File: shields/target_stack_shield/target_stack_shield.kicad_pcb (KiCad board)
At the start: 4 copper layers, 85 x 56 mm, 17 parts, among them IC1 NCP1117DT33T5G, J1 Probe Channel 0, J2 Probe Channel 1, J3 Probe Channel 2, J4 Probe Channel 3, J5 GPIO shield connector 40pin, J6 probe shield connector 20 or 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

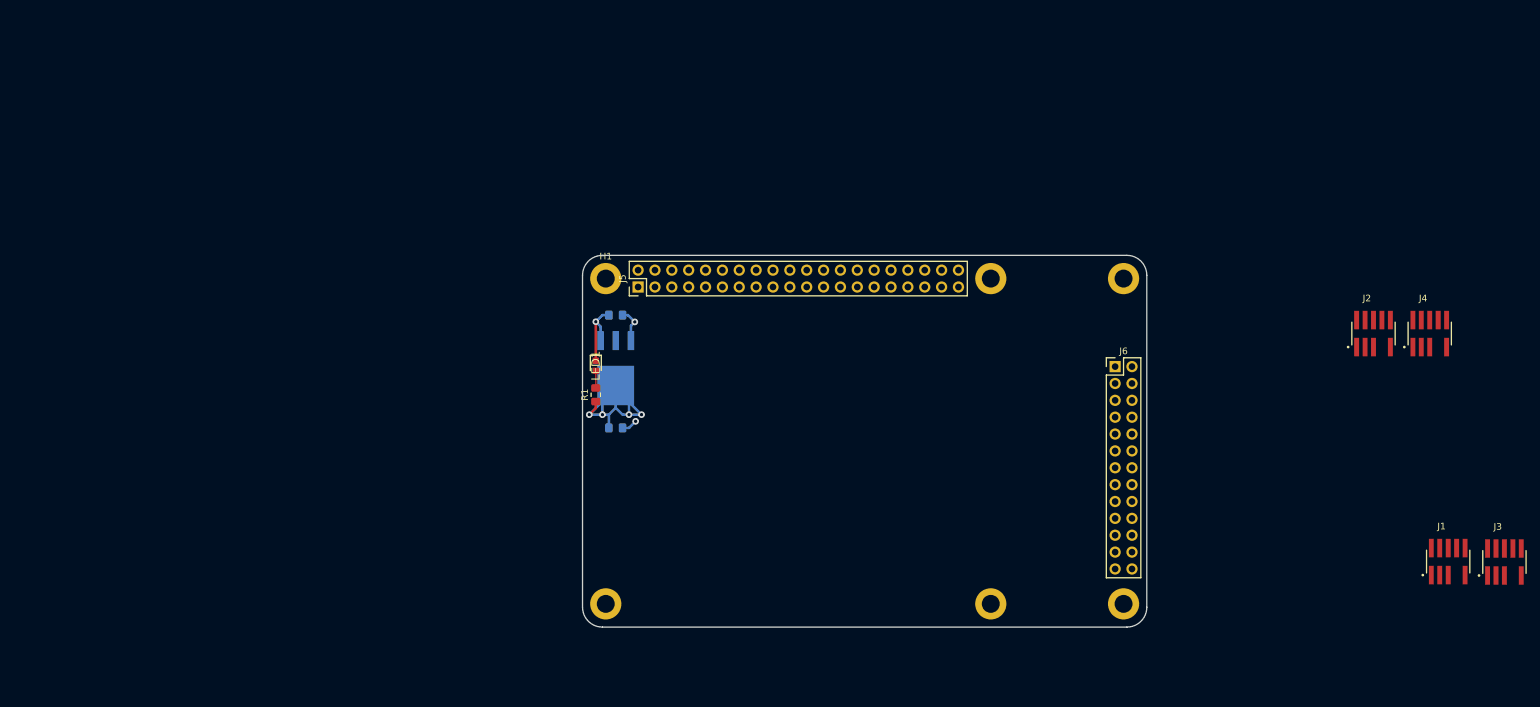
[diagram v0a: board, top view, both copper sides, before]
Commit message: work on target stack shield layout
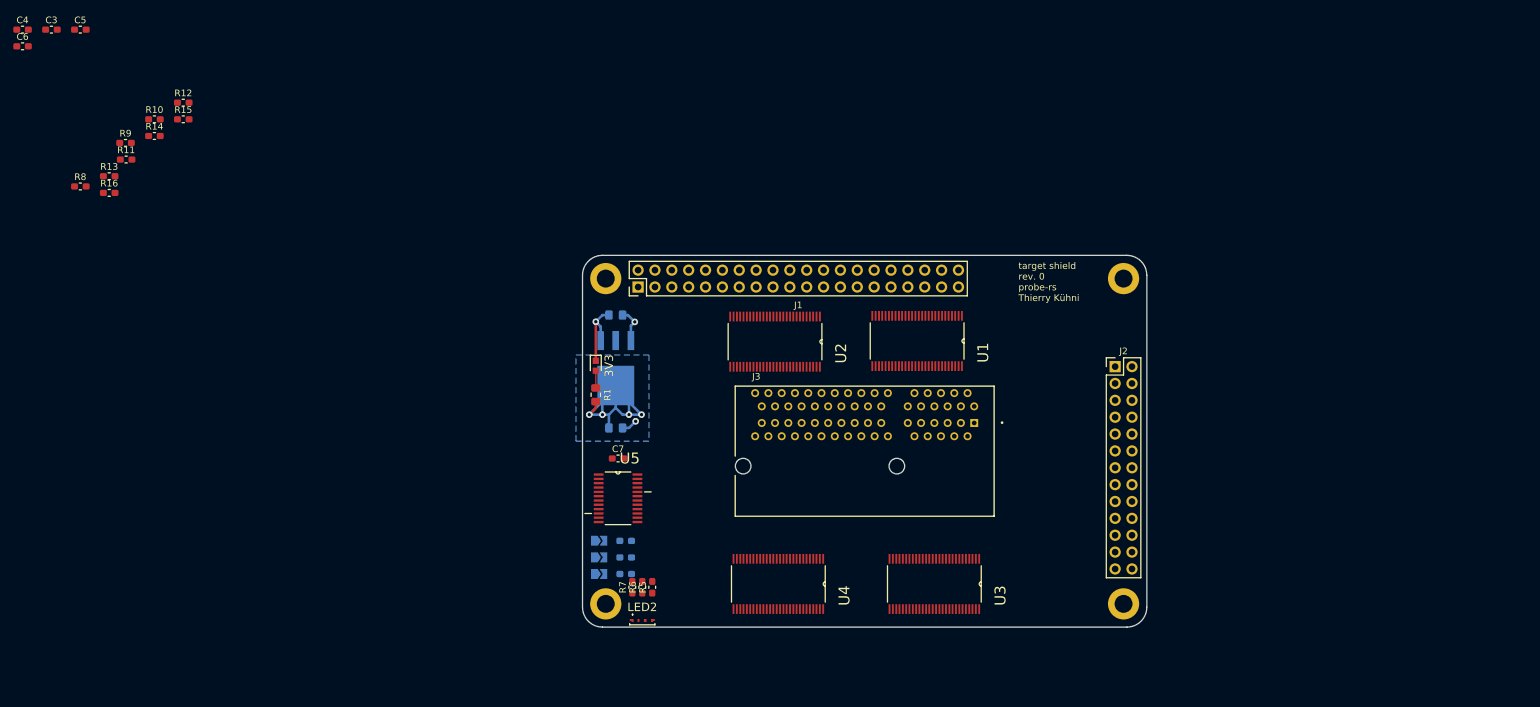
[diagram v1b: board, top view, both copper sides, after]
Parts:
- removed H5, H6: MountingHole, MountingHole:MountingHole_2.7mm_M2.5_DIN965_Pad
- removed J4: Probe Channel 3, hive:SAMTEC_FTSH-105-01-F-DV-007
- removed J5: GPIO shield connector 40pin, Connector_PinHeader_2.54mm:PinHeader_2x20_P2.54mm_Vertical
- removed J6: probe shield connector 20 or 26pin, Connector_PinHeader_2.54mm:PinHeader_2x13_P2.54mm_Vertical
- removed LED1: 3.3V OK (green), hive:LEDC1608X80N
- added 3V3: 3.3V OK (green), hive:LEDC1608X80N, F.Cu at (112.0, 70.6)
- added C3: 100n, Capacitor_SMD:C_0603_1608Metric_Pad1.05x0.95mm_HandSolder, F.Cu at (30.0, 20.0)
- added C4: 100n, Capacitor_SMD:C_0603_1608Metric_Pad1.05x0.95mm_HandSolder, F.Cu at (25.6, 20.0)
- added C5: 100n, Capacitor_SMD:C_0603_1608Metric_Pad1.05x0.95mm_HandSolder, F.Cu at (34.4, 20.0)
- added C6: 100n, Capacitor_SMD:C_0603_1608Metric_Pad1.05x0.95mm_HandSolder, F.Cu at (25.6, 22.5)
- added C7: 100n, Capacitor_SMD:C_0603_1608Metric_Pad1.05x0.95mm_HandSolder, F.Cu at (115.3, 84.6)
- added JP1: Address Bit 0, Jumper:SolderJumper-2_P1.3mm_Open_TrianglePad1.0x1.5mm, B.Cu at (112.5, 102.0)
- added JP2: Address Bit 1, Jumper:SolderJumper-2_P1.3mm_Open_TrianglePad1.0x1.5mm, B.Cu at (112.5, 99.5)
- added JP3: Address Bit 2, Jumper:SolderJumper-2_P1.3mm_Open_TrianglePad1.0x1.5mm, B.Cu at (112.5, 97.0)
- added LED2: KRTB_AILMS1-5B5C-B1B12-0-R18, hive:KRTBAILMS15B5CB1B120R18, F.Cu at (119.0, 109.2)
- added R10: 100k, Resistor_SMD:R_0603_1608Metric_Pad1.05x0.95mm_HandSolder, F.Cu at (45.5, 33.5)
- added R11: 100k, Resistor_SMD:R_0603_1608Metric_Pad1.05x0.95mm_HandSolder, F.Cu at (41.2, 39.6)
- added R12: 100k, Resistor_SMD:R_0603_1608Metric_Pad1.05x0.95mm_HandSolder, F.Cu at (49.9, 31.0)
- added R13: 100k, Resistor_SMD:R_0603_1608Metric_Pad1.05x0.95mm_HandSolder, F.Cu at (38.7, 42.1)
- added R14: 100k, Resistor_SMD:R_0603_1608Metric_Pad1.05x0.95mm_HandSolder, F.Cu at (45.5, 36.0)
- added R15: 100k, Resistor_SMD:R_0603_1608Metric_Pad1.05x0.95mm_HandSolder, F.Cu at (49.9, 33.5)
- added R16: 100k, Resistor_SMD:R_0603_1608Metric_Pad1.05x0.95mm_HandSolder, F.Cu at (38.7, 44.6)
- added R2: 100k, Resistor_SMD:R_0603_1608Metric_Pad1.05x0.95mm_HandSolder, B.Cu at (116.5, 102.0)
- added R3: 100k, Resistor_SMD:R_0603_1608Metric_Pad1.05x0.95mm_HandSolder, B.Cu at (116.5, 99.5)
- added R4: 100k, Resistor_SMD:R_0603_1608Metric_Pad1.05x0.95mm_HandSolder, B.Cu at (116.5, 97.0)
- added R5: 150, Resistor_SMD:R_0603_1608Metric_Pad1.05x0.95mm_HandSolder, F.Cu at (120.5, 104.0)
- added R6: 45, Resistor_SMD:R_0603_1608Metric_Pad1.05x0.95mm_HandSolder, F.Cu at (119.0, 104.0)
- added R7: 30, Resistor_SMD:R_0603_1608Metric_Pad1.05x0.95mm_HandSolder, F.Cu at (117.5, 104.0)
- added R8: 100k, Resistor_SMD:R_0603_1608Metric_Pad1.05x0.95mm_HandSolder, F.Cu at (34.4, 43.6)
- added R9: 100k, Resistor_SMD:R_0603_1608Metric_Pad1.05x0.95mm_HandSolder, F.Cu at (41.2, 37.1)
- added U1: SN74CB3T16211DGGR, hive:SOP50P810X120-56N, F.Cu at (160.4, 66.9)
- added U2: SN74CB3T16211DGGR, hive:SOP50P810X120-56N, F.Cu at (139.0, 67.0)
- added U3: SN74CB3T16211DGGR, hive:SOP50P810X120-56N, F.Cu at (163.0, 103.5)
- added U4: SN74CB3T16211DGGR, hive:SOP50P810X120-56N, F.Cu at (139.5, 103.5)
- added U5: PCA9535CPW,118, hive:SOP65P640X110-24N, F.Cu at (115.3, 90.6)
- H1, H2, H3, H4: value MountingHole -> MountingHole_Pad
- J1: value Probe Channel 0 -> GPIO shield connector 40pin; footprint hive:SAMTEC_FTSH-105-01-F-DV-007 -> hive:PinHeader_2x20_P2.54mm_Vertical_gpio_shield
- J2: value Probe Channel 1 -> probe shield connector 26pin; footprint hive:SAMTEC_FTSH-105-01-F-DV-007 -> hive:PinHeader_2x13_P2.54mm_Vertical_probe_shield
- J3: value Probe Channel 2 -> PCIE-064-02-X-D-RA; footprint hive:SAMTEC_FTSH-105-01-F-DV-007 -> hive:SAMTEC_PCIE-064-02-X-D-RA
- R1: value 65 -> 195
- moved J1 128.8 mm to (118.4, 58.8), turned to 90 degrees
- moved J3 97.8 mm to (152.5, 83.5)
- moved J2 39.2 mm to (190.2, 70.8)
- moved H2 20.0 mm to (191.5, 57.5)
- moved H4 20.0 mm to (191.5, 106.5)
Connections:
- J1 pad 10: /RST_0 -> /UART_RxD1
- J2 pad 10: /RST_1 -> /TDI|NC_1
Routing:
- net +5V: track 20.0 -> 10.1 mm
- net (no net): track 0.00 -> 1.52 mm
- added copper zone on B.Cu, net +3V3
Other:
- board text added: "target shield rev. 0 probe-rs Thierry Kühni"

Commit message: Further work on layout
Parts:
- C3, C4, C5, C6, R10, R11, R12, R13, R14, R15, R16, R8, R9: moved to B.Cu
- moved C3 172.4 mm to (186.0, 93.5), turned to 90 degrees
- moved C4 170.2 mm to (186.0, 77.0), turned to 90 degrees
- moved C5 151.2 mm to (161.0, 102.5)
- moved C6 139.4 mm to (139.9, 102.5)
- moved R8 103.9 mm to (122.0, 99.5)
- moved R9 100.9 mm to (122.0, 97.5)
- moved R10 98.5 mm to (122.0, 95.5)
- moved R11 97.1 mm to (122.0, 93.5)
- moved R13 95.9 mm to (122.0, 89.5)
- moved R12 94.2 mm to (122.0, 91.5)
- moved R14 92.2 mm to (122.0, 87.5)
- moved R16 89.1 mm to (114.5, 91.5), turned to 270 degrees
- moved R15 88.9 mm to (122.0, 85.5)
- moved U2 44.7 mm to (182.5, 77.5), turned to 180 degrees
- moved U1 35.0 mm to (182.5, 94.0), turned to 180 degrees
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- renumbered 3V3 to LED1
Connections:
- R10 pad 1: /Bus switches/BUS_SW_CH2 -> /Bus switches/TARGET_SW_CH1
- R11 pad 1: /Bus switches/BUS_SW_CH3 -> /Bus switches/TARGET_SW_CH0
- R12 pad 1: /Bus switches/TARGET_SW_CH0 -> /Bus switches/BUS_SW_CH3
- R13 pad 1: /Bus switches/TARGET_SW_CH1 -> /Bus switches/BUS_SW_CH2
- R14 pad 1: /Bus switches/TARGET_SW_CH2 -> /Bus switches/BUS_SW_CH1
- R15 pad 1: /Bus switches/TARGET_SW_CH3 -> /Bus switches/BUS_SW_CH0
- R8 pad 1: /Bus switches/BUS_SW_CH0 -> /Bus switches/TARGET_SW_CH3
- R9 pad 1: /Bus switches/BUS_SW_CH1 -> /Bus switches/TARGET_SW_CH2
- U1 pad 15: /TMS|SWDIO_2 -> /RST_2
- U1 pad 16: /TCK|SWDCLK_2 -> /TDI|NC_2
- U1 pad 2: /TMS|SWDIO_3 -> /RST_3
- U1 pad 20: /TDI|NC_2 -> /TCK|SWDCLK_2
- U1 pad 21: /RST_2 -> /TMS|SWDIO_2
- U1 pad 3: /TCK|SWDCLK_3 -> /TDI|NC_3
- U1 pad 36: /Bus switches/BUS_RST -> /Bus switches/BUS_TMS|SWDIO
- U1 pad 37: /Bus switches/BUS_TDI|NC -> /Bus switches/BUS_TCK|SWDCLK
- U1 pad 40: /Bus switches/BUS_TCK|SWDCLK -> /Bus switches/BUS_TDI|NC
- U1 pad 41: /Bus switches/BUS_TMS|SWDIO -> /Bus switches/BUS_RST
- U1 pad 5: /TDI|NC_3 -> /TCK|SWDCLK_3
- U1 pad 50: /Bus switches/BUS_RST -> /Bus switches/BUS_TMS|SWDIO
- U1 pad 51: /Bus switches/BUS_TDI|NC -> /Bus switches/BUS_TCK|SWDCLK
- U1 pad 53: /Bus switches/BUS_TCK|SWDCLK -> /Bus switches/BUS_TDI|NC
- U1 pad 54: /Bus switches/BUS_TMS|SWDIO -> /Bus switches/BUS_RST
- U1 pad 6: /RST_3 -> /TMS|SWDIO_3
- U2 pad 15: /TMS|SWDIO_0 -> /RST_0
- U2 pad 16: /TCK|SWDCLK_0 -> /TDI|NC_0
- U2 pad 2: /TMS|SWDIO_1 -> /RST_1
- U2 pad 20: /TDI|NC_0 -> /TCK|SWDCLK_0
- U2 pad 21: /RST_0 -> /TMS|SWDIO_0
- U2 pad 3: /TCK|SWDCLK_1 -> /TDI|NC_1
- U2 pad 36: /Bus switches/BUS_RST -> /Bus switches/BUS_TMS|SWDIO
- U2 pad 37: /Bus switches/BUS_TDI|NC -> /Bus switches/BUS_TCK|SWDCLK
- U2 pad 40: /Bus switches/BUS_TCK|SWDCLK -> /Bus switches/BUS_TDI|NC
- U2 pad 41: /Bus switches/BUS_TMS|SWDIO -> /Bus switches/BUS_RST
- U2 pad 5: /TDI|NC_1 -> /TCK|SWDCLK_1
- U2 pad 50: /Bus switches/BUS_RST -> /Bus switches/BUS_TMS|SWDIO
- U2 pad 51: /Bus switches/BUS_TDI|NC -> /Bus switches/BUS_TCK|SWDCLK
- U2 pad 53: /Bus switches/BUS_TCK|SWDCLK -> /Bus switches/BUS_TDI|NC
- U2 pad 54: /Bus switches/BUS_TMS|SWDIO -> /Bus switches/BUS_RST
- U2 pad 6: /RST_1 -> /TMS|SWDIO_1
- U3 pad 15: /Bus switches/BUS_TMS|SWDIO -> /Bus switches/BUS_RST
- U3 pad 16: /Bus switches/BUS_TCK|SWDCLK -> /Bus switches/BUS_TDI|NC
- U3 pad 2: /Bus switches/BUS_TMS|SWDIO -> /Bus switches/BUS_RST
- U3 pad 20: /Bus switches/BUS_TDI|NC -> /Bus switches/BUS_TCK|SWDCLK
- U3 pad 21: /Bus switches/BUS_RST -> /Bus switches/BUS_TMS|SWDIO
- U3 pad 3: /Bus switches/BUS_TCK|SWDCLK -> /Bus switches/BUS_TDI|NC
- U3 pad 30: /TGT_UART_RxD0 -> /TGT_UART_RxD1
- U3 pad 31: /TGT_UART_TxD0 -> /TGT_UART_TxD1
- U3 pad 32: /TGT_GPIO0.3 -> /TGT_GPIO1.3
- U3 pad 33: /TGT_GPIO0.2 -> /TGT_GPIO1.2
- U3 pad 34: /TGT_GPIO0.1 -> /TGT_GPIO1.1
- U3 pad 35: /TGT_GPIO0.0 -> /TGT_GPIO1.0
- U3 pad 36: /TGT_RST_0 -> /TGT_TMS|SWDIO_1
- U3 pad 37: /TGT_TDI|NC_0 -> /TGT_TCK|SWDCLK_1
- U3 pad 39: /TGT_TDO|SWO_0 -> /TGT_TDO|SWO_1
- U3 pad 40: /TGT_TCK|SWDCLK_0 -> /TGT_TDI|NC_1
- U3 pad 41: /TGT_TMS|SWDIO_0 -> /TGT_RST_1
- U3 pad 43: /TGT_UART_RxD1 -> /TGT_UART_RxD0
- U3 pad 44: /TGT_UART_TxD1 -> /TGT_UART_TxD0
- U3 pad 45: /TGT_GPIO1.3 -> /TGT_GPIO0.3
- U3 pad 46: /TGT_GPIO1.2 -> /TGT_GPIO0.2
- U3 pad 47: /TGT_GPIO1.1 -> /TGT_GPIO0.1
- U3 pad 48: /TGT_GPIO1.0 -> /TGT_GPIO0.0
- U3 pad 5: /Bus switches/BUS_TDI|NC -> /Bus switches/BUS_TCK|SWDCLK
- U3 pad 50: /TGT_RST_1 -> /TGT_TMS|SWDIO_0
- U3 pad 51: /TGT_TDI|NC_1 -> /TGT_TCK|SWDCLK_0
- U3 pad 52: /TGT_TDO|SWO_1 -> /TGT_TDO|SWO_0
- U3 pad 53: /TGT_TCK|SWDCLK_1 -> /TGT_TDI|NC_0
- U3 pad 54: /TGT_TMS|SWDIO_1 -> /TGT_RST_0
- U3 pad 55: /Bus switches/TARGET_SW_CH0 -> /Bus switches/TARGET_SW_CH1
- U3 pad 56: /Bus switches/TARGET_SW_CH1 -> /Bus switches/TARGET_SW_CH0
- U3 pad 6: /Bus switches/BUS_RST -> /Bus switches/BUS_TMS|SWDIO
- U4 pad 15: /Bus switches/BUS_TMS|SWDIO -> /Bus switches/BUS_RST
- U4 pad 16: /Bus switches/BUS_TCK|SWDCLK -> /Bus switches/BUS_TDI|NC
- U4 pad 2: /Bus switches/BUS_TMS|SWDIO -> /Bus switches/BUS_RST
- U4 pad 20: /Bus switches/BUS_TDI|NC -> /Bus switches/BUS_TCK|SWDCLK
- U4 pad 21: /Bus switches/BUS_RST -> /Bus switches/BUS_TMS|SWDIO
- U4 pad 3: /Bus switches/BUS_TCK|SWDCLK -> /Bus switches/BUS_TDI|NC
- U4 pad 30: /TGT_UART_RxD2 -> /TGT_UART_RxD3
- U4 pad 31: /TGT_UART_TxD2 -> /TGT_UART_TxD3
- U4 pad 32: /TGT_GPIO2.3 -> /TGT_GPIO3.3
- U4 pad 33: /TGT_GPIO2.2 -> /TGT_GPIO3.2
- U4 pad 34: /TGT_GPIO2.1 -> /TGT_GPIO3.1
- U4 pad 35: /TGT_GPIO2.0 -> /TGT_GPIO3.0
- U4 pad 36: /TGT_RST_2 -> /TGT_TMS|SWDIO_3
- U4 pad 37: /TGT_TDI|NC_2 -> /TGT_TCK|SWDCLK_3
- U4 pad 39: /TGT_TDO|SWO_2 -> /TGT_TDO|SWO_3
- U4 pad 40: /TGT_TCK|SWDCLK_2 -> /TGT_TDI|NC_3
- U4 pad 41: /TGT_TMS|SWDIO_2 -> /TGT_RST_3
- U4 pad 43: /TGT_UART_RxD3 -> /TGT_UART_RxD2
- U4 pad 44: /TGT_UART_TxD3 -> /TGT_UART_TxD2
- U4 pad 45: /TGT_GPIO3.3 -> /TGT_GPIO2.3
- U4 pad 46: /TGT_GPIO3.2 -> /TGT_GPIO2.2
- U4 pad 47: /TGT_GPIO3.1 -> /TGT_GPIO2.1
- U4 pad 48: /TGT_GPIO3.0 -> /TGT_GPIO2.0
- U4 pad 5: /Bus switches/BUS_TDI|NC -> /Bus switches/BUS_TCK|SWDCLK
- U4 pad 50: /TGT_RST_3 -> /TGT_TMS|SWDIO_2
- U4 pad 51: /TGT_TDI|NC_3 -> /TGT_TCK|SWDCLK_2
- U4 pad 52: /TGT_TDO|SWO_3 -> /TGT_TDO|SWO_2
- U4 pad 53: /TGT_TCK|SWDCLK_3 -> /TGT_TDI|NC_2
- U4 pad 54: /TGT_TMS|SWDIO_3 -> /TGT_RST_2
- U4 pad 55: /Bus switches/TARGET_SW_CH2 -> /Bus switches/TARGET_SW_CH3
- U4 pad 56: /Bus switches/TARGET_SW_CH3 -> /Bus switches/TARGET_SW_CH2
- U4 pad 6: /Bus switches/BUS_RST -> /Bus switches/BUS_TMS|SWDIO
- U5 pad 13: /Bus switches/BUS_SW_CH0 -> /Bus switches/TARGET_SW_CH3
- U5 pad 14: /Bus switches/BUS_SW_CH1 -> /Bus switches/TARGET_SW_CH2
- U5 pad 15: /Bus switches/BUS_SW_CH2 -> /Bus switches/TARGET_SW_CH1
- U5 pad 16: /Bus switches/BUS_SW_CH3 -> /Bus switches/TARGET_SW_CH0
- U5 pad 17: /Bus switches/TARGET_SW_CH0 -> /Bus switches/BUS_SW_CH3
- U5 pad 18: /Bus switches/TARGET_SW_CH1 -> /Bus switches/BUS_SW_CH2
- U5 pad 19: /Bus switches/TARGET_SW_CH2 -> /Bus switches/BUS_SW_CH1
- U5 pad 20: /Bus switches/TARGET_SW_CH3 -> /Bus switches/BUS_SW_CH0
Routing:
- net /UART_TxD1: track 0.00 -> 74.5 mm, vias 0 -> 2
- net /UART_RxD1: track 0.00 -> 72.0 mm, vias 0 -> 2
- net /GPIO1.0: track 0.00 -> 71.1 mm
- net /UART_TxD0: track 0.00 -> 67.4 mm, vias 0 -> 2
- net /GPIO1.1: track 0.00 -> 67.2 mm
- net /GPIO1.2: track 0.00 -> 65.6 mm
- net /GPIO0.0: track 0.00 -> 63.5 mm, vias 0 -> 2
- net /GPIO1.3: track 0.00 -> 62.2 mm
- net /UART_TxD3: track 0.00 -> 61.4 mm, vias 0 -> 2
- net /UART_TxD2: track 0.00 -> 61.2 mm, vias 0 -> 4
- net /GPIO0.1: track 0.00 -> 60.3 mm, vias 0 -> 2
- net /UART_RxD2: track 0.00 -> 60.3 mm, vias 0 -> 4
- net /GPIO2.0: track 0.00 -> 59.9 mm, vias 0 -> 1
- net /GPIO2.1: track 0.00 -> 59.3 mm, vias 0 -> 1
- net /GPIO0.2: track 0.00 -> 58.6 mm, vias 0 -> 2
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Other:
- net class I2C: clearance 0.54 -> 0.2

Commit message: finished target stack shield layout
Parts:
- R1: footprint Resistor_SMD:R_0805_2012Metric_Pad1.15x1.40mm_HandSolder -> Resistor_SMD:R_0603_1608Metric_Pad1.05x0.95mm_HandSolder
- moved C5 0.77 mm to (160.9, 103.3)
- moved C6 0.53 mm to (139.7, 103.0)
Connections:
- J3 pad A07: /TGT_UART_TxD0 -> /TGT_RST_0
- J3 pad A08: /TGT_UART_RxD0 -> /TGT_TDI|NC_0
- J3 pad A09: /TGT_GPIO0.0 -> /TGT_TDO|SWO_0
- J3 pad A10: /TGT_GPIO0.1 -> /TGT_TCK|SWDCLK_0
- J3 pad A11: /TGT_GPIO0.2 -> /TGT_TMS|SWDIO_0
- J3 pad A12: /TGT_GPIO0.3 -> GND
- J3 pad A13: GND -> /TGT_GPIO0.0
- J3 pad A14: /TGT_TCK|SWDCLK_0 -> /TGT_GPIO0.1
- J3 pad A15: /TGT_TMS|SWDIO_0 -> /TGT_GPIO0.2
- J3 pad A16: /TGT_TDO|SWO_0 -> /TGT_GPIO0.3
- J3 pad A17: /TGT_TDI|NC_0 -> /TGT_UART_TxD0
- J3 pad A18: /TGT_RST_0 -> /TGT_UART_RxD0
- J3 pad A20: /TGT_UART_TxD2 -> /TGT_RST_2
- J3 pad A21: /TGT_UART_RxD2 -> /TGT_TDI|NC_2
- J3 pad A22: /TGT_GPIO2.0 -> /TGT_TDO|SWO_2
- J3 pad A23: /TGT_GPIO2.1 -> /TGT_TCK|SWDCLK_2
- J3 pad A24: /TGT_GPIO2.2 -> /TGT_TMS|SWDIO_2
- J3 pad A25: /TGT_GPIO2.3 -> GND
- J3 pad A26: GND -> /TGT_GPIO2.0
- J3 pad A27: /TGT_TCK|SWDCLK_2 -> /TGT_GPIO2.1
- J3 pad A28: /TGT_TMS|SWDIO_2 -> /TGT_GPIO2.2
- J3 pad A29: /TGT_TDO|SWO_2 -> /TGT_GPIO2.3
- J3 pad A30: /TGT_TDI|NC_2 -> /TGT_UART_TxD2
- J3 pad A31: /TGT_RST_2 -> /TGT_UART_RxD2
- J3 pad B07: /TGT_UART_TxD1 -> /TGT_UART_RxD1
- J3 pad B08: /TGT_UART_RxD1 -> /TGT_UART_TxD1
- J3 pad B09: /TGT_GPIO1.0 -> /TGT_GPIO1.3
- J3 pad B10: /TGT_GPIO1.1 -> /TGT_GPIO1.2
- J3 pad B11: /TGT_GPIO1.2 -> /TGT_GPIO1.1
- J3 pad B12: /TGT_GPIO1.3 -> /TGT_GPIO1.0
- J3 pad B14: /TGT_TCK|SWDCLK_1 -> /TGT_TMS|SWDIO_1
- J3 pad B15: /TGT_TMS|SWDIO_1 -> /TGT_TCK|SWDCLK_1
- J3 pad B20: /TGT_UART_TxD3 -> /TGT_UART_RxD3
- J3 pad B21: /TGT_UART_RxD3 -> /TGT_UART_TxD3
- J3 pad B22: /TGT_GPIO3.0 -> /TGT_GPIO3.3
- J3 pad B23: /TGT_GPIO3.1 -> /TGT_GPIO3.2
- J3 pad B24: /TGT_GPIO3.2 -> /TGT_GPIO3.1
- J3 pad B25: /TGT_GPIO3.3 -> /TGT_GPIO3.0
- J3 pad B27: /TGT_TCK|SWDCLK_3 -> /TGT_TMS|SWDIO_3
- J3 pad B28: /TGT_TMS|SWDIO_3 -> /TGT_TCK|SWDCLK_3
- U3 pad 10: /Bus switches/BUS_GPIO2 -> /Bus switches/BUS_TCK|SWDCLK
- U3 pad 11: /Bus switches/BUS_GPIO3 -> /Bus switches/BUS_TDO|SWO
- U3 pad 12: /Bus switches/BUS_UART_TxD -> /Bus switches/BUS_TDI|NC
- U3 pad 13: /Bus switches/BUS_UART_RxD -> /Bus switches/BUS_RST
- U3 pad 2: /Bus switches/BUS_RST -> /Bus switches/BUS_UART_RxD
- U3 pad 3: /Bus switches/BUS_TDI|NC -> /Bus switches/BUS_UART_TxD
- U3 pad 4: /Bus switches/BUS_TDO|SWO -> /Bus switches/BUS_GPIO3
- U3 pad 43: /TGT_UART_RxD0 -> /TGT_RST_0
- U3 pad 44: /TGT_UART_TxD0 -> /TGT_TDI|NC_0
- U3 pad 45: /TGT_GPIO0.3 -> /TGT_TDO|SWO_0
- U3 pad 46: /TGT_GPIO0.2 -> /TGT_TCK|SWDCLK_0
- U3 pad 47: /TGT_GPIO0.1 -> /TGT_TMS|SWDIO_0
- U3 pad 5: /Bus switches/BUS_TCK|SWDCLK -> /Bus switches/BUS_GPIO2
- U3 pad 50: /TGT_TMS|SWDIO_0 -> /TGT_GPIO0.1
- U3 pad 51: /TGT_TCK|SWDCLK_0 -> /TGT_GPIO0.2
- U3 pad 52: /TGT_TDO|SWO_0 -> /TGT_GPIO0.3
- U3 pad 53: /TGT_TDI|NC_0 -> /TGT_UART_TxD0
- U3 pad 54: /TGT_RST_0 -> /TGT_UART_RxD0
- U3 pad 6: /Bus switches/BUS_TMS|SWDIO -> /Bus switches/BUS_GPIO1
- U3 pad 9: /Bus switches/BUS_GPIO1 -> /Bus switches/BUS_TMS|SWDIO
- U4 pad 10: /Bus switches/BUS_GPIO2 -> /Bus switches/BUS_TCK|SWDCLK
- U4 pad 11: /Bus switches/BUS_GPIO3 -> /Bus switches/BUS_TDO|SWO
- U4 pad 12: /Bus switches/BUS_UART_TxD -> /Bus switches/BUS_TDI|NC
- U4 pad 13: /Bus switches/BUS_UART_RxD -> /Bus switches/BUS_RST
- U4 pad 2: /Bus switches/BUS_RST -> /Bus switches/BUS_UART_RxD
- U4 pad 3: /Bus switches/BUS_TDI|NC -> /Bus switches/BUS_UART_TxD
- U4 pad 4: /Bus switches/BUS_TDO|SWO -> /Bus switches/BUS_GPIO3
- U4 pad 43: /TGT_UART_RxD2 -> /TGT_RST_2
- U4 pad 44: /TGT_UART_TxD2 -> /TGT_TDI|NC_2
- U4 pad 45: /TGT_GPIO2.3 -> /TGT_TDO|SWO_2
- U4 pad 46: /TGT_GPIO2.2 -> /TGT_TCK|SWDCLK_2
- U4 pad 47: /TGT_GPIO2.1 -> /TGT_TMS|SWDIO_2
- U4 pad 5: /Bus switches/BUS_TCK|SWDCLK -> /Bus switches/BUS_GPIO2
- U4 pad 50: /TGT_TMS|SWDIO_2 -> /TGT_GPIO2.1
- U4 pad 51: /TGT_TCK|SWDCLK_2 -> /TGT_GPIO2.2
- U4 pad 52: /TGT_TDO|SWO_2 -> /TGT_GPIO2.3
- U4 pad 53: /TGT_TDI|NC_2 -> /TGT_UART_TxD2
- U4 pad 54: /TGT_RST_2 -> /TGT_UART_RxD2
- U4 pad 6: /Bus switches/BUS_TMS|SWDIO -> /Bus switches/BUS_GPIO1
- U4 pad 9: /Bus switches/BUS_GPIO1 -> /Bus switches/BUS_TMS|SWDIO
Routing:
- net /Bus switches/BUS_UART_RxD: track 36.3 -> 141.8 mm, vias 1 -> 4
- net /Bus switches/BUS_SW_CH0: track 6.16 -> 102.7 mm, vias 1 -> 4
- net /Bus switches/BUS_GPIO3: track 36.9 -> 132.7 mm, vias 1 -> 4
- net /Bus switches/BUS_UART_TxD: track 36.5 -> 131.2 mm, vias 1 -> 4
- net /Bus switches/BUS_SW_CH1: track 4.66 -> 98.6 mm, vias 1 -> 4
- net /Bus switches/BUS_GPIO1: track 35.7 -> 128.3 mm, vias 0 -> 4
- net /Bus switches/BUS_GPIO2: track 35.6 -> 125.1 mm, vias 0 -> 4
- net /Bus switches/BUS_GPIO0: track 35.7 -> 119.0 mm, vias 0 -> 4
- net /Bus switches/BUS_TMS|SWDIO: track 34.1 -> 117.1 mm, vias 0 -> 4
- net /Bus switches/BUS_SW_CH2: track 3.45 -> 82.8 mm, vias 1 -> 4
- net /Bus switches/BUS_SW_CH3: track 2.90 -> 81.8 mm, vias 1 -> 4
- net /Bus switches/BUS_TCK|SWDCLK: track 34.1 -> 109.9 mm, vias 0 -> 4
- net /Bus switches/BUS_TDO|SWO: track 33.2 -> 108.5 mm, vias 0 -> 4
- net /Bus switches/BUS_TDI|NC: track 33.6 -> 102.0 mm, vias 0 -> 4
- net /Bus switches/BUS_RST: track 33.4 -> 98.3 mm, vias 0 -> 3
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
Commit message: updates on silkscreen, added 3d renders
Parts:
- added G***: LOGO, hive:probe-rs-logo, F.Cu at (178.6, 57.4)
- added REF**: solder-jumper-instruction, hive:solder-jumper-instruction, F.Cu at (139.8, 93.9)
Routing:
- net /BOARD_DETECT: track 71.7 -> 62.4 mm
- net GND: track 84.9 -> 92.5 mm, vias 45 -> 50
- net +3V3: vias 19 -> 21
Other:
- board text added: "3V3"
- board text added: "STATUS"
- board text added: "Target stack shield rev. 0 Thierry Kühni"
- board text removed: "target shield rev. 0 probe-rs Thierry Kühni"

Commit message: fixed broken silkscreen
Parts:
- moved REF** 0.38 mm to (139.8, 93.5)
